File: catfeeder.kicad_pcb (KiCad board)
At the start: 2 copper layers, 40.1 x 66.9 mm, 88 parts, among them J1 Barrel_Jack_Switch, J2 USB_B_Mini, J3 RFID, J4 DoorOpen, J5 Scale, J6 Auger Motor, J7 Door Motor, J8 DoorClose, M1 Mount, M2 Mount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

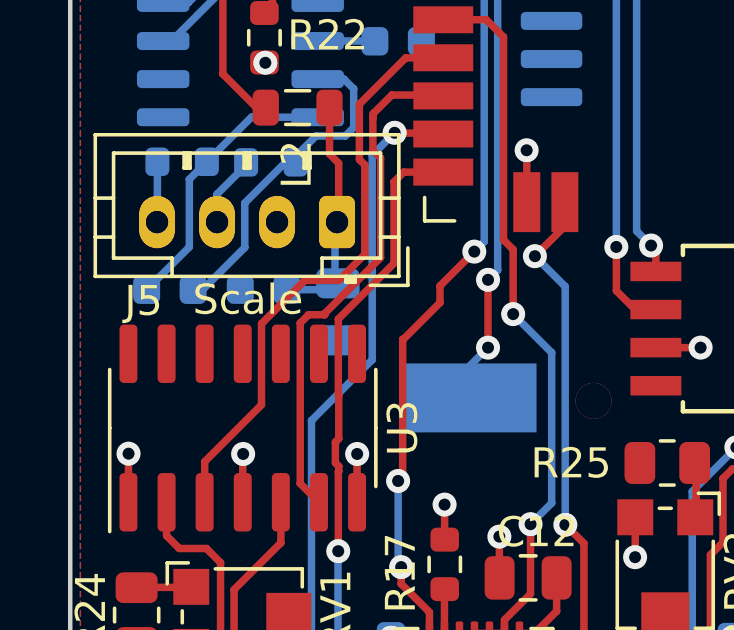
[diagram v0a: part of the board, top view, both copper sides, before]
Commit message: Save with new KiCAD version. Cleanup some tracks and vias.
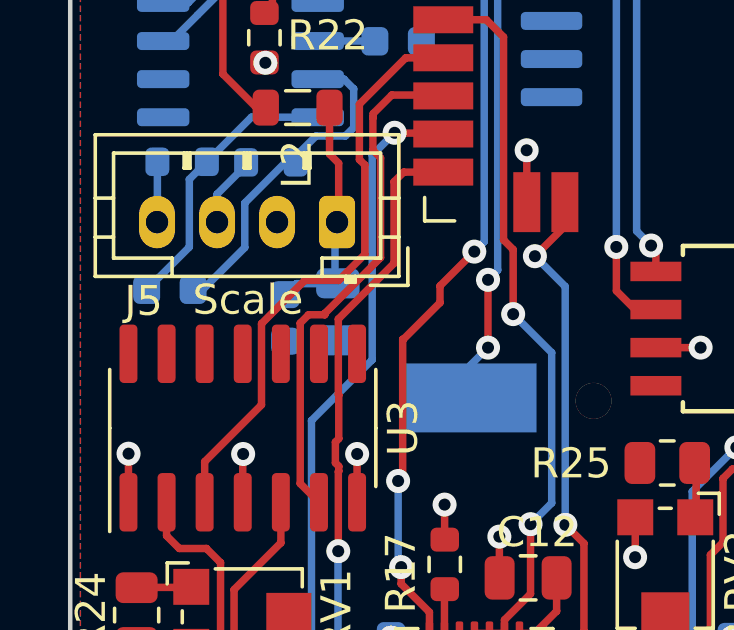
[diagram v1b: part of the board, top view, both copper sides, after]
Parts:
- C27: value 0.1uF -> 10uF
- moved C19 1.19 mm to (84.8, 128.2), turned to -90 degrees
